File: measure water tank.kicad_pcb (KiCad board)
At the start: 2 copper layers, 14 parts, among them J1 Jack-DC, J2 Conn_ARM_SWD_TagConnect_TC2030, U1 SPX3819M5-L, U2 SPX3819M5-L, U3 ESP32-S3-MINI-1U

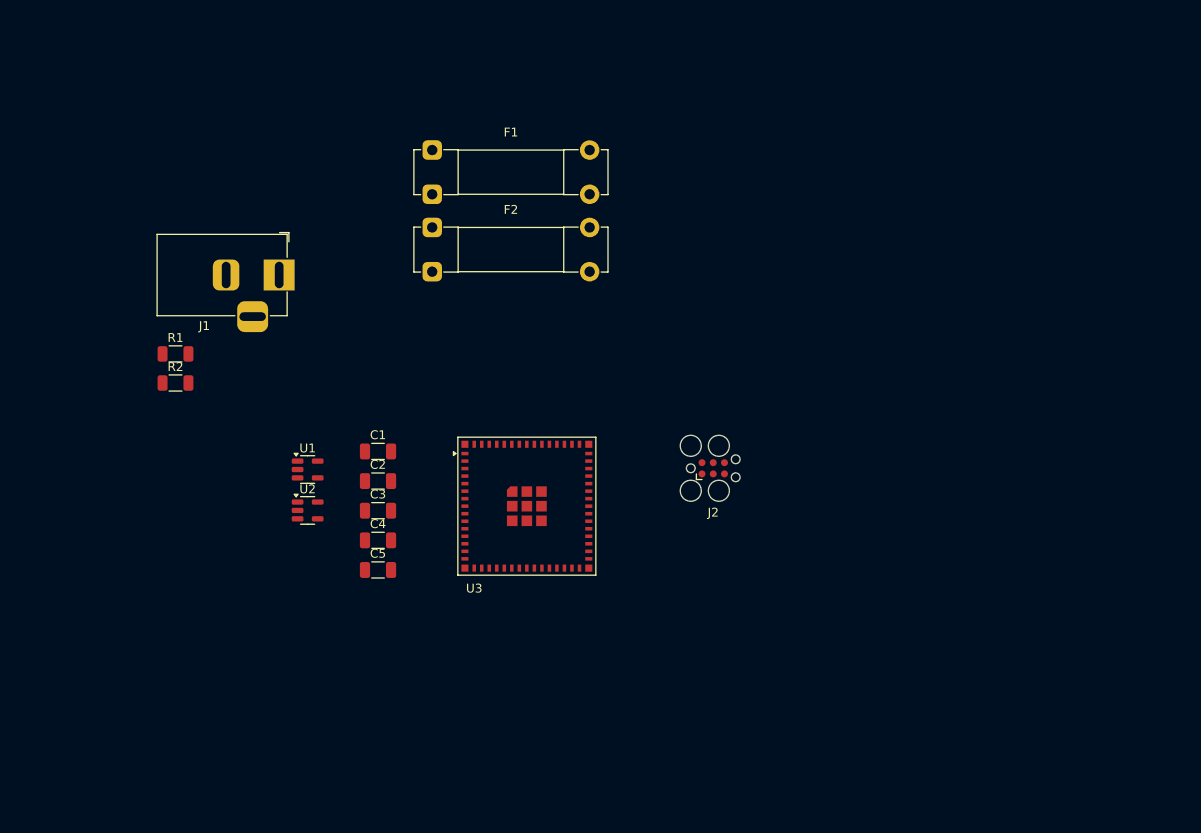
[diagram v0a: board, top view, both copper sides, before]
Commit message: add: ch340 changed: esp32
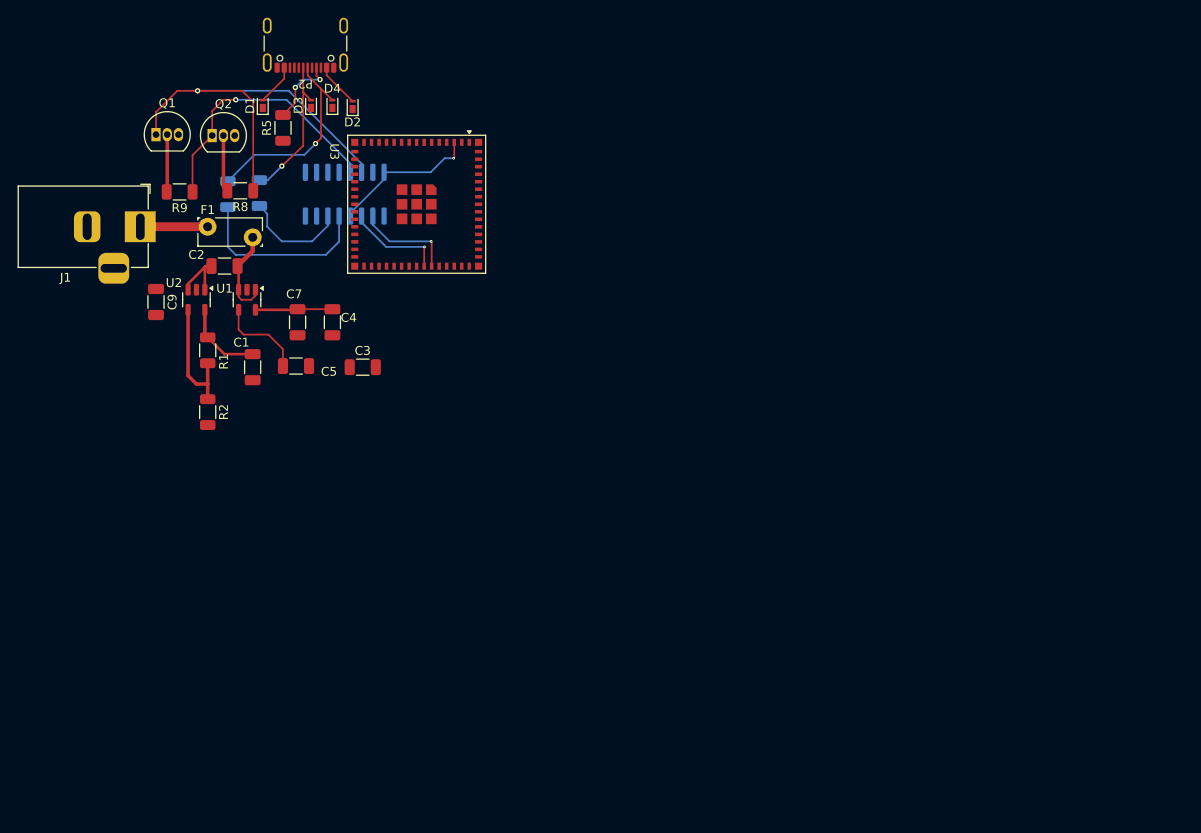
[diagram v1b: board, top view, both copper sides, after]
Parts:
- removed F2: 600mA, Fuse:Fuseholder_Clip-5x20mm_Bel_FC-203-22_Lateral_P17.80x5.00mm_D1.17mm_Horizontal
- removed J2: Conn_ARM_SWD_TagConnect_TC2030, Connector:Tag-Connect_TC2030-IDC-FP_2x03_P1.27mm_Vertical
- added C7: 0.1nF/25v, Capacitor_SMD:C_1206_3216Metric, F.Cu at (101.6, 48.9)
- added C9: 0.1uf, Capacitor_SMD:C_1206_3216Metric, F.Cu at (85.6, 46.6)
- added D1: LESD5D5.0CT1G, Diode_SMD:Nexperia_DSN1608-2_1.6x0.8mm, F.Cu at (97.7, 24.4)
- added D2: LESD5D5.0CT1G, Diode_SMD:Nexperia_DSN1608-2_1.6x0.8mm, F.Cu at (107.8, 24.5)
- added D3: LESD5D5.0CT1G, Diode_SMD:Nexperia_DSN1608-2_1.6x0.8mm, F.Cu at (103.1, 24.4)
- added D4: LESD5D5.0CT1G, Diode_SMD:Nexperia_DSN1608-2_1.6x0.8mm, F.Cu at (105.5, 24.4)
- added P2: USB_C_Plug_USB2.0, Connector_USB:USB_C_Receptacle_GCT_USB4105-xx-A_16P_TopMnt_Horizontal, F.Cu at (102.5, 16.4)
- added Q1: S8050, Package_TO_SOT_THT:TO-92_Inline, F.Cu at (85.6, 27.7)
- added Q2: S8050, Package_TO_SOT_THT:TO-92_Inline, F.Cu at (91.9, 27.8)
- added R3: 0ohm, Resistor_SMD:R_1206_3216Metric, B.Cu at (97.3, 34.3)
- added R4: 0ohm, Resistor_SMD:R_1206_3216Metric, B.Cu at (93.7, 34.4)
- added R5: 5.1k, Resistor_SMD:R_1206_3216Metric, F.Cu at (99.9, 26.9)
- added R8: 12k, Resistor_SMD:R_1206_3216Metric, F.Cu at (95.1, 34.0)
- added R9: 12k, Resistor_SMD:R_1206_3216Metric, F.Cu at (88.3, 34.2)
- added U5: CH340C, Package_SO:SOIC-16_3.9x9.9mm_P1.27mm, B.Cu at (106.9, 34.4)
- C4: value 1uf -> 10nF/6.3V
- C5: value 10nF -> 470pf
- F1: footprint Fuse:Fuseholder_Clip-5x20mm_Bel_FC-203-22_Lateral_P17.80x5.00mm_D1.17mm_Horizontal -> Fuse:Fuse_Bourns_MF-RG300
- moved U3 36.3 mm to (115.1, 35.6), turned to -90 degrees
- moved C2 29.9 mm to (93.3, 42.5), turned to 180 degrees
- moved U2 26.9 mm to (90.2, 46.4), turned to -90 degrees
- moved F1 26.8 mm to (91.4, 38.1)
- moved C4 25.2 mm to (105.5, 48.9), turned to -90 degrees
- moved C5 24.8 mm to (101.4, 53.8)
- moved U1 20.4 mm to (95.9, 46.4), turned to -90 degrees
- moved C1 17.1 mm to (96.5, 54.0), turned to -90 degrees
- moved J1 16.6 mm to (83.8, 38.1)
- moved C3 16.3 mm to (109.0, 54.0)
- moved R2 4.91 mm to (91.4, 59.1), turned to -90 degrees
- moved R1 3.66 mm to (91.4, 52.1), turned to -90 degrees
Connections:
- net Net-(C2-Pad1) renamed usb_5v
- C3 pad 1: Net-(C3-Pad1) -> +12V
- C3 pad 2: Net-(U1-EN) -> GND
- U1 pad 1: Net-(U1-EN) -> +12V
- U1 pad 3: Net-(U1-EN) -> +12V
- U3 pad 39: unconnected-(U3-TXD0-Pad39) -> ch340c-rx
- U3 pad 40: unconnected-(U3-RXD0-Pad40) -> ch340c-tx
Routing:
- net ch340c-rst: track 0.00 -> 48.0 mm, vias 0 -> 1
- net ch340c-dtr: track 0.00 -> 30.2 mm, vias 0 -> 1
- net +3v3: track 0.00 -> 25.6 mm, vias 0 -> 1
- net Net-(D4-A): track 0.00 -> 22.9 mm, vias 0 -> 1
- net usb_dp: track 0.00 -> 21.0 mm
- net Net-(D3-A): track 0.00 -> 16.7 mm, vias 0 -> 1
- net Net-(U2-ADJ): track 0.00 -> 14.1 mm
- net usb_dn: track 0.00 -> 12.1 mm
- net ch340c-tx: track 0.00 -> 11.2 mm, vias 0 -> 1
- net ch340c-rx: track 0.00 -> 11.2 mm, vias 0 -> 1
- net usb_5v: track 0.00 -> 10.4 mm
- net Net-(U1-ADJ): track 0.00 -> 10.1 mm
- net Net-(D1-A): track 0.00 -> 9.67 mm
- net +5v: track 0.00 -> 9.11 mm
- net Net-(P2-CC): track 0.00 -> 8.36 mm, vias 0 -> 2
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
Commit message: add: protector de estatica
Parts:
- removed C9: 0.1uf, Capacitor_SMD:C_1206_3216Metric
- added C6: 0.1nF/25v, Capacitor_SMD:C_1206_3216Metric, F.Cu at (198.0, 71.7)
- added R7: 5.1k, Resistor_SMD:R_1206_3216Metric, F.Cu at (197.0, 87.0)
- Q1, Q2: footprint Package_TO_SOT_THT:TO-92_Inline -> Package_TO_SOT_SMD:SOT-23
- R3, R4, U5: moved to F.Cu
- moved Q1 115.0 mm to (188.6, 78.9), turned to -90 degrees
- moved P2 114.1 mm to (188.2, 91.7), turned to 0 degrees
- moved D1 111.5 mm to (192.2, 83.5), turned to 180 degrees
- moved Q2 104.9 mm to (183.6, 78.9), turned to -90 degrees
- moved U1 102.9 mm to (193.5, 78.9), turned to 90 degrees
- moved D3 102.8 mm to (187.3, 83.5), turned to 0 degrees
- moved D2 101.0 mm to (189.8, 83.5), turned to 0 degrees
- moved R4 100.6 mm to (180.0, 86.0), turned to 180 degrees
- moved R9 100.3 mm to (179.0, 77.0), turned to -90 degrees
- moved C5 99.4 mm to (197.6, 79.0), turned to -90 degrees
- moved D4 98.9 mm to (184.8, 83.5), turned to 0 degrees
- moved R3 96.0 mm to (180.0, 83.0), turned to 180 degrees
- moved C3 92.9 mm to (197.0, 83.5)
- moved R8 91.6 mm to (176.0, 77.0), turned to 90 degrees
- moved J1 91.0 mm to (161.5, 85.5), turned to 90 degrees
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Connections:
- C2 pad 1: usb_5v -> Net-(C2-Pad1)
- C3 pad 1: +12V -> usb_5v
- F1 pad 1: +12V -> usb_5v
- F1 pad 2: usb_5v -> Net-(C2-Pad1)
- J1 pad 1: +12V -> usb_5v
- P2 pad A4: Net-(D1-A) -> Net-(U4-VCC)
- P2 pad A6: Net-(D4-A) -> Net-(P2-D+)
- P2 pad A7: Net-(D3-A) -> Net-(P2-D-)
- P2 pad A9: Net-(D1-A) -> Net-(U4-VCC)
- P2 pad B4: Net-(D1-A) -> Net-(U4-VCC)
- P2 pad B5: unconnected-(P2-VCONN-PadB5) -> Net-(P2-VCONN)
- P2 pad B9: Net-(D1-A) -> Net-(U4-VCC)
- Q1 pad 3: esp_rst -> EN
- R3 pad 1: Net-(D3-A) -> Net-(P2-D-)
- R4 pad 1: Net-(D4-A) -> Net-(P2-D+)
- U1 pad 1: +12V -> usb_5v
- U1 pad 3: +12V -> usb_5v
- U3 pad 4: unconnected-(U3-IO0-Pad4) -> Gpio0
- U3 pad 45: unconnected-(U3-EN-Pad45) -> EN
- U5 pad 16: +3v3 -> VDDA33A
- U5 pad 4: +3v3 -> VDDA33A
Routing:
- net VDDA33A: track 0.00 -> 65.9 mm
- net Gpio0: track 0.00 -> 35.1 mm, vias 0 -> 2
- net ch340c-rst: track 48.0 -> 20.9 mm, vias 1 -> 0
- net +3v3: track 25.6 -> 0.00 mm, vias 1 -> 0
- net ch340c-dtr: track 30.2 -> 12.6 mm, vias 1 -> 0
- net Net-(D4-A): track 22.9 -> 9.97 mm, vias 1 -> 0
- net Net-(P2-CC): track 8.36 -> 0.00 mm, vias 2 -> 0
- net Net-(P2-VCONN): track 0.00 -> 7.99 mm, vias 0 -> 2
- net Net-(U2-ADJ): track 14.1 -> 6.53 mm
- net +12V: track 7.38 -> 0.00 mm
- net Net-(D1-A): track 9.67 -> 16.6 mm
- net Net-(U1-ADJ): track 10.1 -> 3.18 mm
- net usb_dn: track 12.1 -> 18.9 mm, vias 0 -> 2
- net usb_5v: track 10.4 -> 16.2 mm
- net +5v: track 9.11 -> 3.60 mm
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
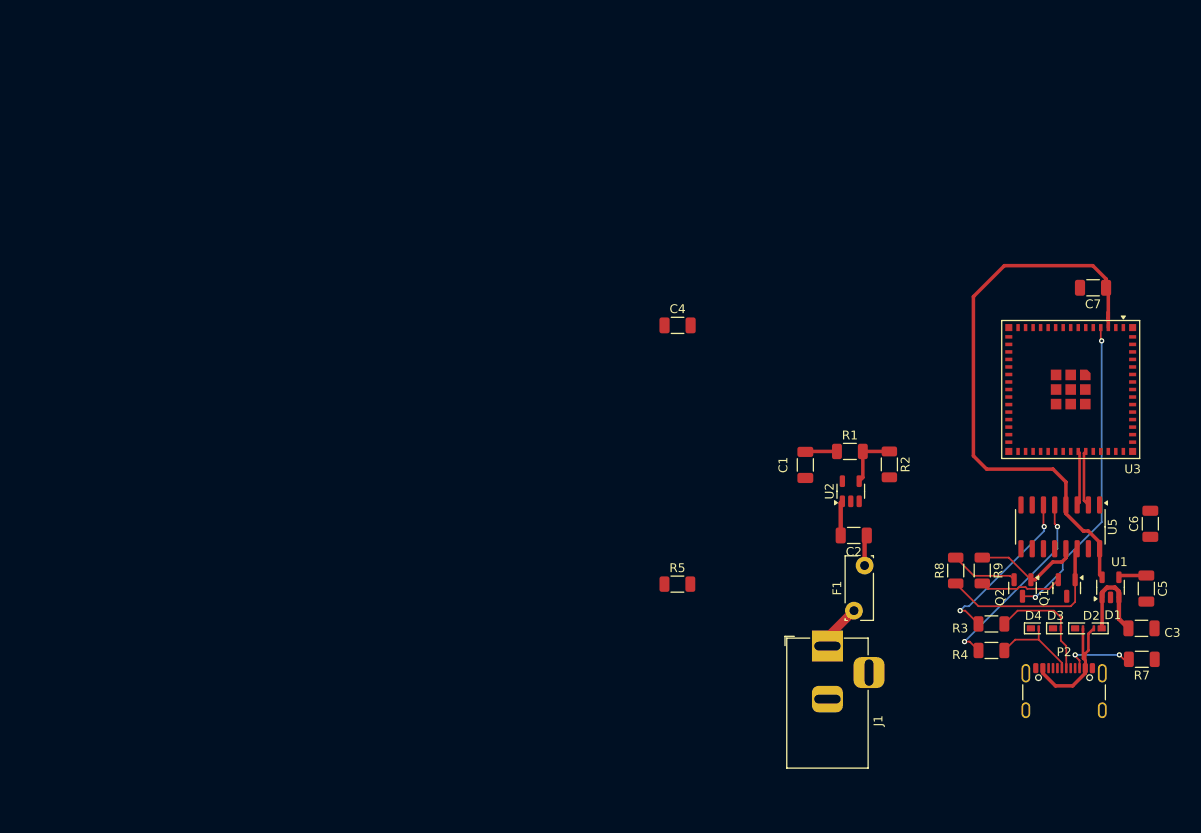
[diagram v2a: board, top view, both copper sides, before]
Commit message: del: elimine el ch340 y conecte el usb directamente
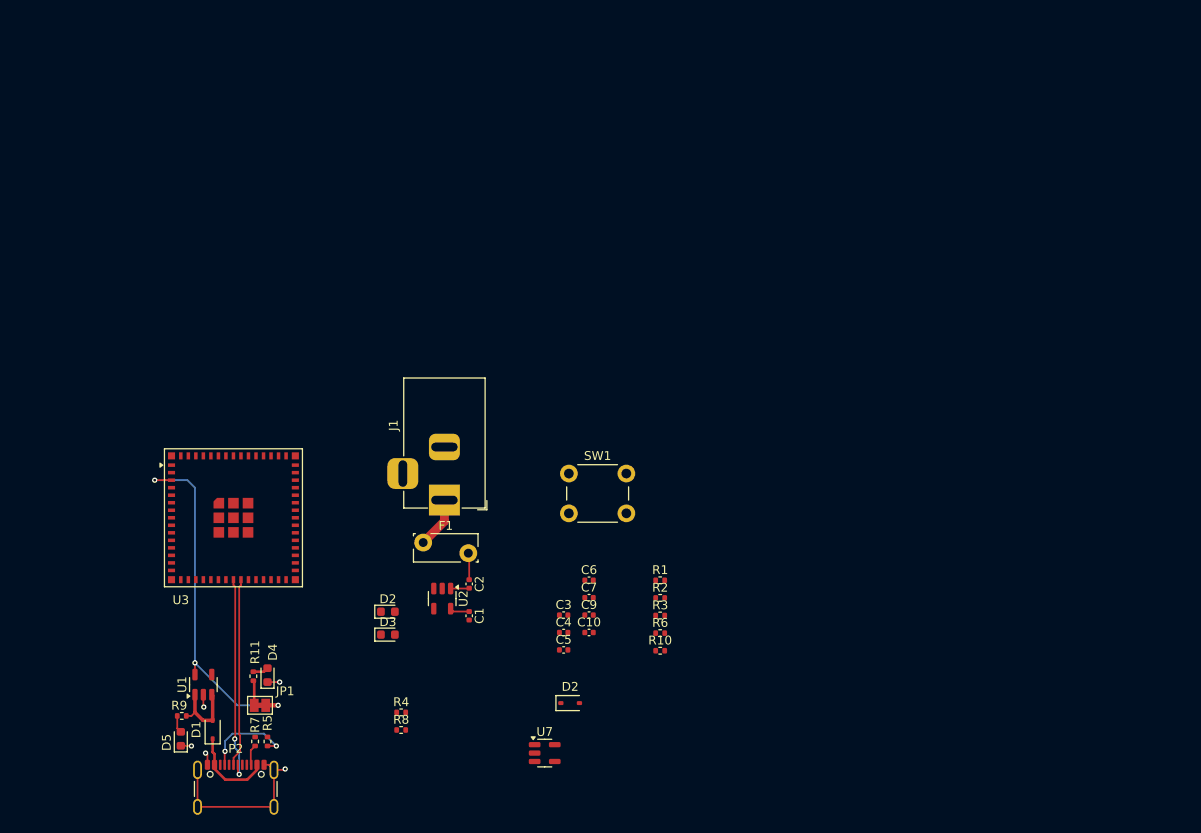
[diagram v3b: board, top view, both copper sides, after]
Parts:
- removed the D2 at (189.8, 83.5)
- removed Q1, Q2: S8050, Package_TO_SOT_SMD:SOT-23
- removed U5: CH340C, Package_SO:SOIC-16_3.9x9.9mm_P1.27mm
- added C10: 0.1uF, Capacitor_SMD:C_0402_1005Metric, F.Cu at (134.6, 84.0)
- added C9: 2.2uF, Capacitor_SMD:C_0402_1005Metric, F.Cu at (134.6, 82.0)
- added D2: BAT60A, Diode_SMD:D_SOD-323, F.Cu at (132.4, 92.0)
- added D2: yellow, LED_SMD:LED_0603_1608Metric, F.Cu at (111.8, 81.6)
- added D5: purple, LED_SMD:LED_0603_1608Metric, F.Cu at (88.4, 96.0)
- added JP1: ~, Jumper:SolderJumper-2_P1.3mm_Bridged_Pad1.0x1.5mm, F.Cu at (97.3, 92.2)
- added R10: 100k, Resistor_SMD:R_0402_1005Metric, F.Cu at (142.6, 86.0)
- added R11: 4.7k, Resistor_SMD:R_0402_1005Metric, F.Cu at (96.6, 88.9)
- added R6: 0, Resistor_SMD:R_0402_1005Metric, F.Cu at (142.6, 84.0)
- added SW1: SW_Push, Button_Switch_THT:SW_PUSH_6mm, F.Cu at (132.3, 66.0)
- added U7: RT9080-3.3, Package_TO_SOT_SMD:SOT-23-5, F.Cu at (129.5, 97.6)
- C1, C2, C3, C4, C5, C6, C7: footprint Capacitor_SMD:C_1206_3216Metric -> Capacitor_SMD:C_0402_1005Metric
- D1: value LESD5D5.0CT1G -> BAT60A; footprint Diode_SMD:Nexperia_DSN1608-2_1.6x0.8mm -> Diode_SMD:D_SOD-323
- D3: value LESD5D5.0CT1G -> Red; footprint Diode_SMD:Nexperia_DSN1608-2_1.6x0.8mm -> LED_SMD:LED_0603_1608Metric
- D4: value LESD5D5.0CT1G -> blue; footprint Diode_SMD:Nexperia_DSN1608-2_1.6x0.8mm -> LED_SMD:LED_0603_1608Metric
- R1, R2, R5, R7: footprint Resistor_SMD:R_1206_3216Metric -> Resistor_SMD:R_0402_1005Metric
- R3: value 0ohm -> 10k; footprint Resistor_SMD:R_1206_3216Metric -> Resistor_SMD:R_0402_1005Metric
- R4: value 0ohm -> 4.7k; footprint Resistor_SMD:R_1206_3216Metric -> Resistor_SMD:R_0402_1005Metric
- R8, R9: value 12k -> 4.7k; footprint Resistor_SMD:R_1206_3216Metric -> Resistor_SMD:R_0402_1005Metric
- moved U1 103.1 mm to (91.0, 89.9)
- moved D1 100.9 mm to (92.0, 95.0), turned to 90 degrees
- moved R7 100.7 mm to (96.8, 96.3), turned to -90 degrees
- moved U3 95.8 mm to (94.3, 71.0), turned to 0 degrees
- moved P2 94.3 mm to (94.6, 102.6)
- moved R9 92.0 mm to (88.5, 93.4), turned to 180 degrees
- moved D4 86.7 mm to (98.2, 88.8), turned to 90 degrees
- moved D3 75.5 mm to (111.8, 84.2)
- moved R4 67.1 mm to (113.3, 93.0), turned to 0 degrees
- moved C7 66.9 mm to (134.6, 80.0), turned to 0 degrees
- moved C5 66.2 mm to (131.7, 85.9), turned to 0 degrees
- moved C3 65.3 mm to (131.7, 82.0)
- moved R8 65.2 mm to (113.3, 95.0), turned to 0 degrees
- moved C6 63.8 mm to (134.6, 78.1), turned to 0 degrees
- moved R5 49.6 mm to (98.2, 96.3), turned to -90 degrees
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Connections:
- C1 pad 1: +5v -> Net-(U2-OUT)
- C2 pad 2: Net-(U2-EN) -> Net-(U2-IN)
- C3 pad 1: usb_5v -> VUSB
- D1 pad 1: usb_5v -> Net-(D1-Pad1)
- D1 pad 2: Net-(D1-A) -> VUSB
- D3 pad 1: GND -> VUSB
- F1 pad 1: usb_5v -> +12V
- J1 pad 1: usb_5v -> +12V
- P2 pad A4: Net-(U4-VCC) -> Net-(D1-Pad1)
- P2 pad A6: Net-(P2-D+) -> d+
- P2 pad A7: Net-(P2-D-) -> d-
- P2 pad A9: Net-(U4-VCC) -> Net-(D1-Pad1)
- P2 pad B4: Net-(U4-VCC) -> Net-(D1-Pad1)
- P2 pad B9: Net-(U4-VCC) -> Net-(D1-Pad1)
- R1 pad 1: +5v -> Net-(U2-OUT)
- R3 pad 1: Net-(P2-D-) -> +3v3
- R3 pad 2: usb_dn -> EN
- R4 pad 1: Net-(P2-D+) -> +12V
- R4 pad 2: usb_dp -> Net-(D3-A)
- R8 pad 1: ch340c-rst -> Net-(D2-A)
- R8 pad 2: Net-(Q2-B) -> Net-(U2-OUT)
- R9 pad 1: ch340c-dtr -> VUSB
- U1 pad 1: usb_5v -> VUSB
- U1 pad 3: usb_5v -> VUSB
- U2 pad 1: Net-(U2-EN) -> Net-(U2-IN)
- U2 pad 3: Net-(U2-EN) -> led_control
- U2 pad 5: +5v -> Net-(U2-OUT)
- U3 pad 12: unconnected-(U3-IO8-Pad12) -> ESP8/SDA
- U3 pad 13: unconnected-(U3-IO9-Pad13) -> ESP9/SCL
- U3 pad 23: unconnected-(U3-IO19-Pad23) -> d-
- U3 pad 24: unconnected-(U3-IO20-Pad24) -> d+
- U3 pad 39: ch340c-rx -> unconnected-(U3-TXD0-Pad39)
- U3 pad 40: ch340c-tx -> unconnected-(U3-RXD0-Pad40)
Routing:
- net VDDA33A: track 65.9 -> 0.00 mm
- net +3v3: track 0.00 -> 41.1 mm, vias 0 -> 3
- net Gpio0: track 35.1 -> 0.00 mm, vias 2 -> 0
- net GND: track 0.00 -> 25.1 mm, vias 0 -> 5
- net d-: track 0.00 -> 23.4 mm, vias 0 -> 2
- net usb_dp: track 21.9 -> 0.00 mm, vias 2 -> 0
- net d+: track 0.00 -> 21.4 mm
- net ch340c-rst: track 20.9 -> 0.00 mm
- net usb_dn: track 18.9 -> 0.00 mm, vias 2 -> 0
- net Net-(D1-A): track 16.6 -> 0.00 mm
- net usb_5v: track 16.2 -> 0.00 mm
- net Net-(D3-A): track 13.3 -> 0.00 mm
- net ch340c-dtr: track 12.6 -> 0.00 mm
- net Net-(P2-CC): track 0.00 -> 10.4 mm, vias 0 -> 2
- net Net-(D1-Pad1): track 0.00 -> 9.80 mm
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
